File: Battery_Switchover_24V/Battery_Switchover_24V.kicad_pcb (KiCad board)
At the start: 2 copper layers, 260.5 x 131 mm, 105 parts, among them J1 USB_C_Receptacle_USB2.0_14P, M1 Fan, Q1 PZT2222AT1G, SW1 SW_Push, U10 ACS37002LMABTR-066B5, U11 LM60CIM3, U12 L5973D, U13 AMS1117-3.3, U14 OPA2197xD, U15 FDBL86066-F085, U2 FDBL86066-F085, U3 LPC11U14FBD48-201, U4 LM74610QDGKRQ1, U5 FDBL86066-F085, U6 LM74610QDGKRQ1, U7 FDBL86066-F085, U8 ACS37002LMABTR-066B5, U9 ACS37002LMABTR-066B5, Y1 12.000MHz

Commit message: Added 6 Pin ATX Connector
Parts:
- removed BT2, BT4, BT5, BT6: Battery_Cell, TerminalBlock_RND:TerminalBlock_RND_205-00023_1x02_P10.00mm_Horizontal
- added J10: 10845060, footprints:CONN_SDA_42002-xxxxx_06_MOL, F.Cu at (31.1, 127.3)
- added J11: 10845060, footprints:CONN_SDA_42002-xxxxx_06_MOL, F.Cu at (31.1, 149.4)
- added J3: 10845060, footprints:CONN_SDA_42002-xxxxx_06_MOL, F.Cu at (34.1, 35.5)
- added J4: 10845060, footprints:CONN_SDA_42002-xxxxx_06_MOL, F.Cu at (34.1, 57.6)
- added J5: 10845060, footprints:CONN_SDA_42002-xxxxx_06_MOL, F.Cu at (34.1, 79.7)
- added J6: 10845060, footprints:CONN_SDA_42002-xxxxx_06_MOL, F.Cu at (265.5, 95.6)
- added J7: 10845060, footprints:CONN_SDA_42002-xxxxx_06_MOL, F.Cu at (265.5, 121.3)
- added J8: 10845060, footprints:CONN_SDA_42002-xxxxx_06_MOL, F.Cu at (265.5, 147.1)
- added J9: 10845060, footprints:CONN_SDA_42002-xxxxx_06_MOL, F.Cu at (31.1, 105.3)
- J1: footprint Connector_USB:USB_C_Receptacle_G-Switch_GT-USB-7010ASV -> Connector_USB:USB_C_Receptacle_G-Switch_GT-USB-7051x
- moved C27 125.1 mm to (84.8, 72.2), turned to 0 degrees
- moved C28 121.5 mm to (88.1, 72.2), turned to 180 degrees
- moved C22 117.3 mm to (89.1, 75.7), turned to 0 degrees
- moved U8 113.0 mm to (86.3, 85.2), turned to 90 degrees
- moved R14 111.2 mm to (93.1, 77.7), turned to -90 degrees
- moved C26 103.9 mm to (104.3, 72.8), turned to 0 degrees
- moved C29 100.8 mm to (107.6, 72.8), turned to 180 degrees
- moved C24 96.7 mm to (108.3, 76.1), turned to 0 degrees
- moved R15 92.1 mm to (112.1, 77.0), turned to -90 degrees
- moved U9 89.2 mm to (105.8, 86.6), turned to 90 degrees
- moved C25 86.5 mm to (123.3, 73.7), turned to 0 degrees
- moved C30 84.2 mm to (126.5, 73.7), turned to 180 degrees
- moved C2 83.5 mm to (152.0, 96.3)
- moved C3 83.5 mm to (152.0, 98.5)
- moved C4 83.5 mm to (162.7, 87.8)
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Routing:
- net Net-(D6-A2): track 107.0 -> 0.00 mm
- net Vbatt: track 106.1 -> 0.00 mm
- net Net-(U3-USB_DM): track 42.2 -> 0.00 mm, vias 2 -> 0
- net Net-(U3-USB_DP): track 42.2 -> 0.00 mm
- net Net-(U15-G): track 33.0 -> 0.00 mm, vias 2 -> 0
- net +5V: track 20.0 -> 0.00 mm
- net Vin: track 15.3 -> 0.00 mm
- net Net-(U3-XTALIN): track 13.3 -> 0.00 mm
- net Net-(U3-XTALOUT): track 13.1 -> 0.00 mm
- net +3.3V: track 12.0 -> 0.00 mm
- net Net-(J1-D--PadA7): track 10.6 -> 0.00 mm
- net Net-(J1-CC1): track 10.2 -> 0.00 mm
- net VREF3: track 9.66 -> 0.00 mm
- net Net-(U6-VCAPH): track 9.19 -> 0.00 mm
- net Net-(U4-VCAPH): track 8.22 -> 0.00 mm
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- removed copper zone on F.Cu, net Load1
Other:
- board size 260.5 x 131 mm -> 260.5 x 89 mm

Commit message: Changed PCB size Changed output connector
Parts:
- removed BT3: Battery_Cell, TerminalBlock_RND:TerminalBlock_RND_205-00023_1x02_P10.00mm_Horizontal
- removed J10, J11, J3, J6, J7, J8, J9: 10845060, footprints:CONN_SDA_42002-xxxxx_06_MOL
- added J2: 430450612, footprints:CONN_SD-43045-005_06_MOL, F.Cu at (83.0, 110.0)
- added R20: 4K7, Resistor_SMD:R_0603_1608Metric, F.Cu at (124.7, 98.8)
- J4, J5: value 10845060 -> 430450612; footprint footprints:CONN_SDA_42002-xxxxx_06_MOL -> footprints:CONN_SD-43045-005_06_MOL
- moved C22 151.6 mm to (228.2, 136.0)
- moved C24 151.6 mm to (247.5, 136.4)
- moved C26 151.6 mm to (243.5, 133.2)
- moved C27 151.6 mm to (224.0, 132.5)
- moved C28 151.6 mm to (227.2, 132.5)
- moved C29 151.6 mm to (246.7, 133.2)
- moved R14 151.6 mm to (232.2, 138.0)
- moved R15 151.6 mm to (251.2, 137.4)
- moved U8 151.6 mm to (225.5, 145.5)
- moved U9 151.6 mm to (245.0, 146.9)
- moved U10 123.7 mm to (243.6, 83.4)
- moved J4 79.6 mm to (83.0, 120.4)
- moved R17 72.4 mm to (149.4, 75.6)
- moved D8 71.1 mm to (168.6, 110.7)
- moved J5 70.8 mm to (83.0, 130.8)
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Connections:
- J4 pad 1: GNDPWR2 -> GND
- J4 pad 2: GNDPWR2 -> GND
- J4 pad 3: GNDPWR2 -> GND
- J4 pad 4: Load2 -> Vsupply
- J4 pad 5: Load2 -> Vsupply
- J4 pad 6: Load2 -> Vsupply
- J5 pad 1: GNDPWR1 -> GND
- J5 pad 2: GNDPWR1 -> GND
- J5 pad 3: GNDPWR1 -> GND
- J5 pad 4: Load1 -> Vsupply
- J5 pad 5: Load1 -> Vsupply
- J5 pad 6: Load1 -> Vsupply
- U3 pad 18: unconnected-(U3-PIO1_23-Pad18) -> Temp_data
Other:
- board size 260.5 x 89 mm -> 150.1 x 89 mm

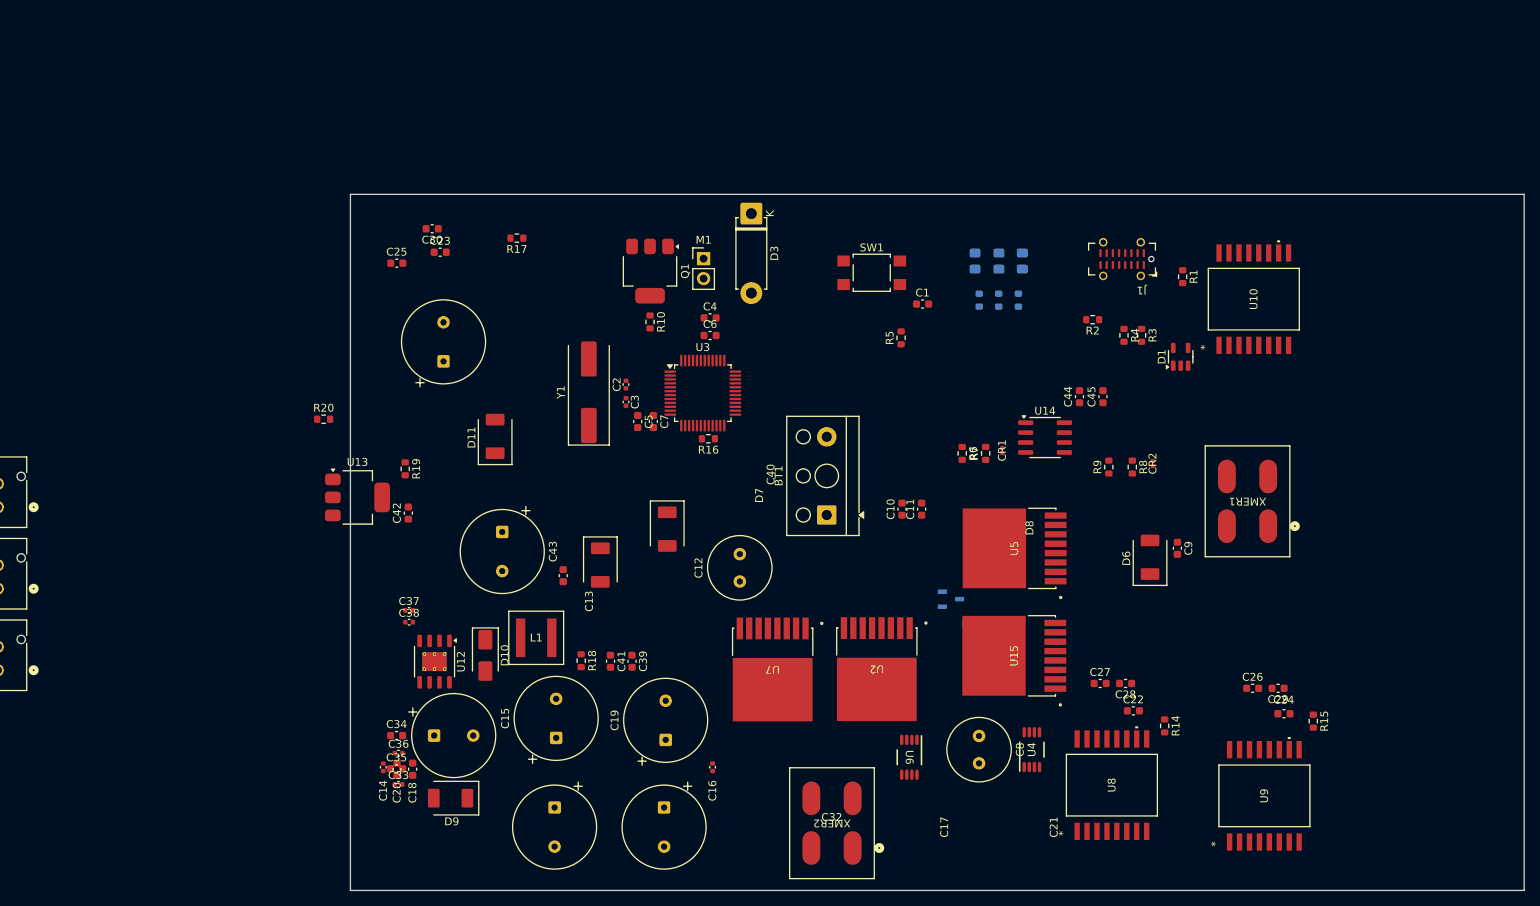
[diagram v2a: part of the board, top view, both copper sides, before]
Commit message: adding BMS and changed topology
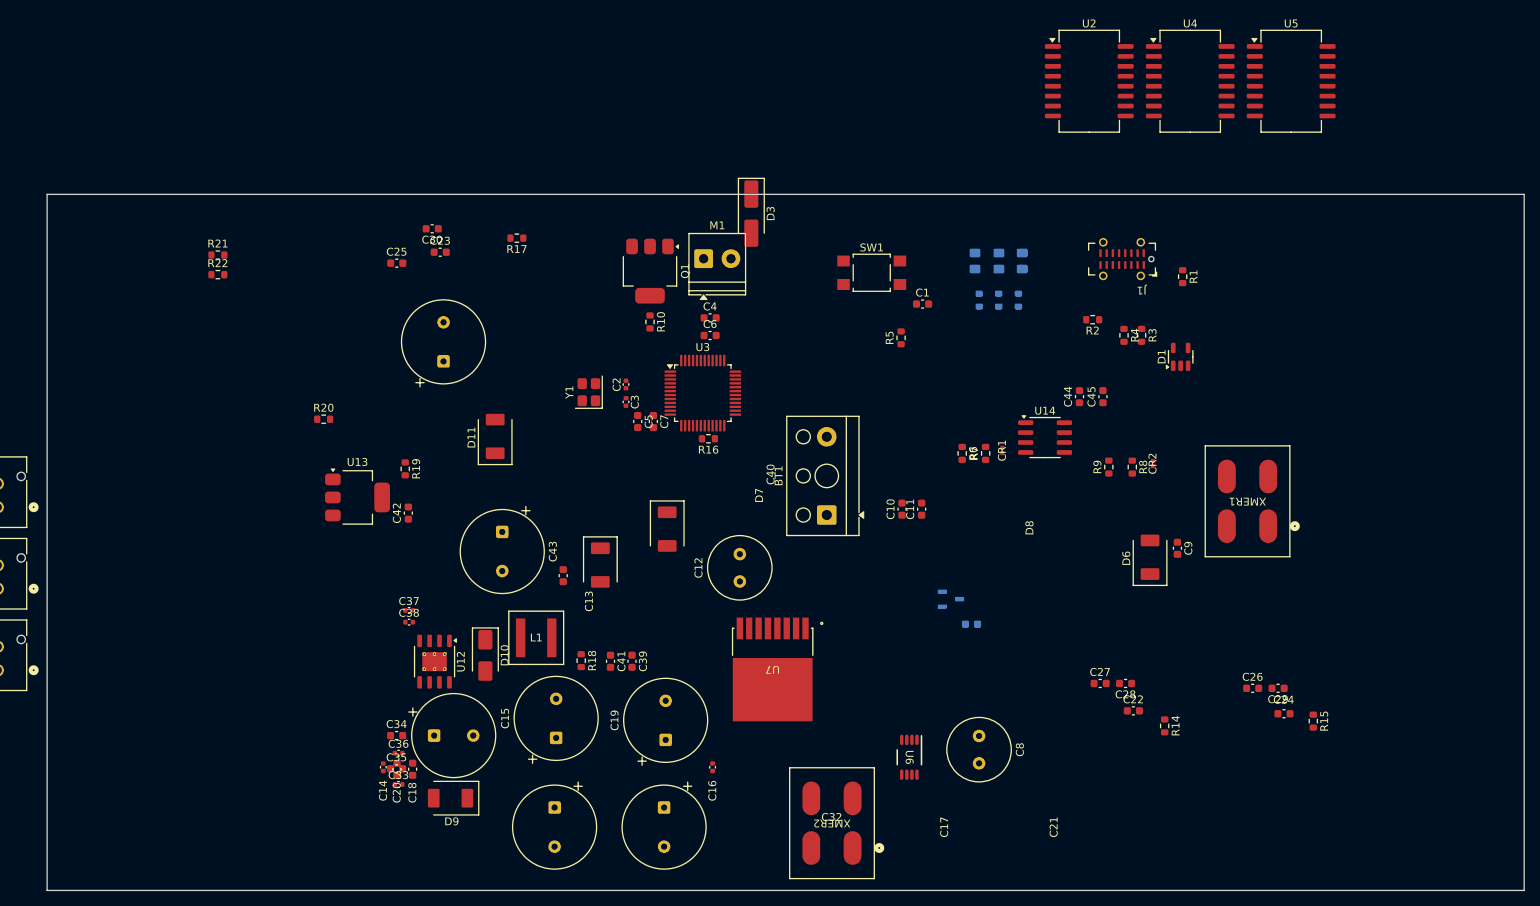
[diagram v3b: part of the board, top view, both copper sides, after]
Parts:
- removed U10, U8, U9: ACS37002LMABTR-066B5, footprints:SOICW16_MC_ALM
- removed U15: FDBL86066-F085, footprints:H-PSOF8L_ONS
- added R21: 4K7, Resistor_SMD:R_0603_1608Metric, F.Cu at (111.1, 77.8)
- added R22: 4K7, Resistor_SMD:R_0603_1608Metric, F.Cu at (111.1, 80.3)
- C1: value 1nF -> 10nF
- C6, C7: value 10uF -> 1uF
- D3: footprint Diode_THT:D_5W_P10.16mm_Horizontal -> Diode_SMD:D_SMA_Handsoldering
- M1: footprint Connector_PinHeader_2.54mm:PinHeader_1x02_P2.54mm_Vertical -> TerminalBlock_Phoenix:TerminalBlock_Phoenix_PT-1,5-2-3.5-H_1x02_P3.50mm_Horizontal
- R10: value 500 -> 10K
- R5: value 10K -> 1K
- U2, U5: value FDBL86066-F085 -> ACS37002; footprint footprints:H-PSOF8L_ONS -> Package_SO:SOIC-16W_7.5x12.8mm_P1.27mm
- U4: value LM74610QDGKRQ1 -> ACS37002; footprint footprints:DGK0008A_N -> Package_SO:SOIC-16W_7.5x12.8mm_P1.27mm
- Y1: footprint Crystal:Crystal_SMD_HC49-SD -> Crystal:Crystal_SMD_TXC_7M-4Pin_3.2x2.5mm
- moved U4 87.8 mm to (235.5, 55.5), turned to 0 degrees
- moved U2 79.9 mm to (222.6, 55.5), turned to 0 degrees
- moved U5 69.4 mm to (248.4, 55.5), turned to 0 degrees
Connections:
- C1 pad 1: Net-(C1-Pad1) -> RESET
- C8 pad 1: Net-(U4-VCAPH) -> unconnected-(C8-Pad1)
- C8 pad 2: Net-(U4-VCAPL) -> unconnected-(C8-Pad2)
- C9 pad 1: Net-(D6-A2) -> Net-(C9-Pad1)
- D1 pad 1: +5V -> Net-(D12-A)
- D6 pad 2: Net-(D6-A2) -> Vin
- J1 pad A4: +5V -> Net-(D12-A)
- J1 pad A9: +5V -> Net-(D12-A)
- J1 pad B4: +5V -> Net-(D12-A)
- J1 pad B9: +5V -> Net-(D12-A)
- R14 pad 2: Net-(U8-*OCF) -> Net-(U2-*OCF)
- R15 pad 2: Net-(U9-*OCF) -> Net-(U4-*OCF)
- R16 pad 2: Net-(U10-*OCF) -> Net-(U5-*OCF)
- R5 pad 1: RESET -> +3.3V
- R5 pad 2: Net-(C1-Pad1) -> RESET
- SW1 pad 1: 3.3V -> GND
- SW1 pad 2: Net-(C1-Pad1) -> RESET
- U2 pad 1: Net-(U2-G) -> Load1
- U2 pad 2: Vbatt -> Load1
- U2 pad 3: Vbatt -> Load1
- U2 pad 4: Vbatt -> Load1
- U2 pad 5: Vbatt -> GNDPWR1
- U2 pad 6: Vbatt -> GNDPWR1
- U2 pad 7: Vbatt -> GNDPWR1
- U2 pad 8: Vbatt -> GNDPWR1
- U2 pad 9: Net-(D6-A2) -> Net-(U2-*OCF)
- U4 pad 1: Net-(U4-VCAPL) -> Load2
- U4 pad 2: Net-(U15-G) -> Load2
- U4 pad 3: unconnected-(U4-NC-Pad3) -> Load2
- U4 pad 4: Net-(D6-A2) -> Load2
- U4 pad 5: unconnected-(U4-NC-Pad5) -> GNDPWR2
- U4 pad 6: Net-(U15-G) -> GNDPWR2
- U4 pad 7: Net-(U4-VCAPH) -> GNDPWR2
- U4 pad 8: Vbatt -> GNDPWR2
- U5 pad 1: Net-(U15-G) -> Load3
- U5 pad 2: Net-(D6-A2) -> Load3
- U5 pad 3: Net-(D6-A2) -> Load3
- U5 pad 4: Net-(D6-A2) -> Load3
- U5 pad 5: Net-(D6-A2) -> GNDPWR3
- U5 pad 6: Net-(D6-A2) -> GNDPWR3
- U5 pad 7: Net-(D6-A2) -> GNDPWR3
- U5 pad 8: Net-(D6-A2) -> GNDPWR3
- U5 pad 9: Vbatt -> Net-(U5-*OCF)
- U6 pad 2: Net-(U2-G) -> Net-(U6-GATE_DRIVE)
- U6 pad 6: Net-(U2-G) -> Net-(U6-GATE_DRIVE)
- U6 pad 8: Net-(D6-A2) -> Net-(U6-CATHODE)
- U7 pad 1: Net-(U2-G) -> Net-(U6-GATE_DRIVE)
- U7 pad 9: Net-(D6-A2) -> Net-(U6-CATHODE)
- XMER1 pad 4: Net-(D6-A2) -> Net-(C9-Pad1)
- XMER2 pad 1: Net-(D6-A2) -> Net-(U6-CATHODE)
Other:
- board size 150.1 x 89 mm -> 188.9 x 89 mm

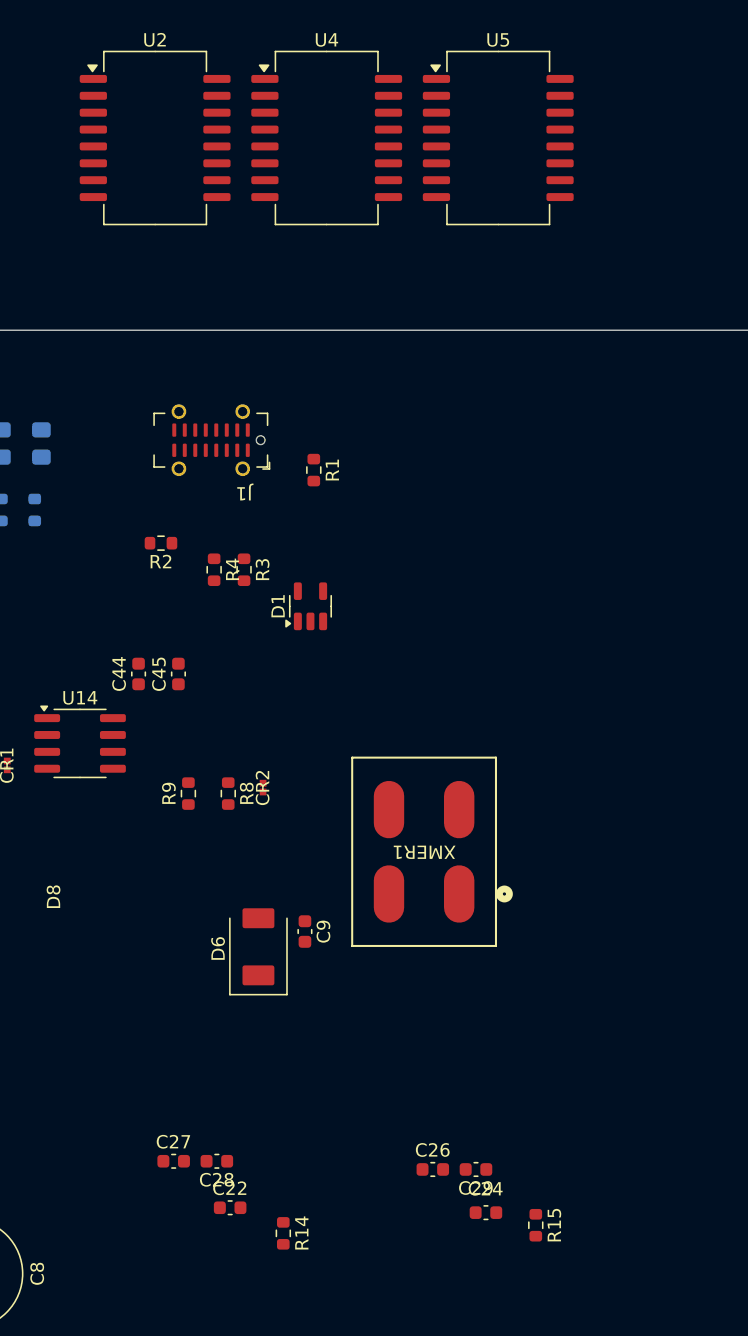
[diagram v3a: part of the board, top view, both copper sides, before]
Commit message: Changed current sensor (fewer analog pins), added extra adc
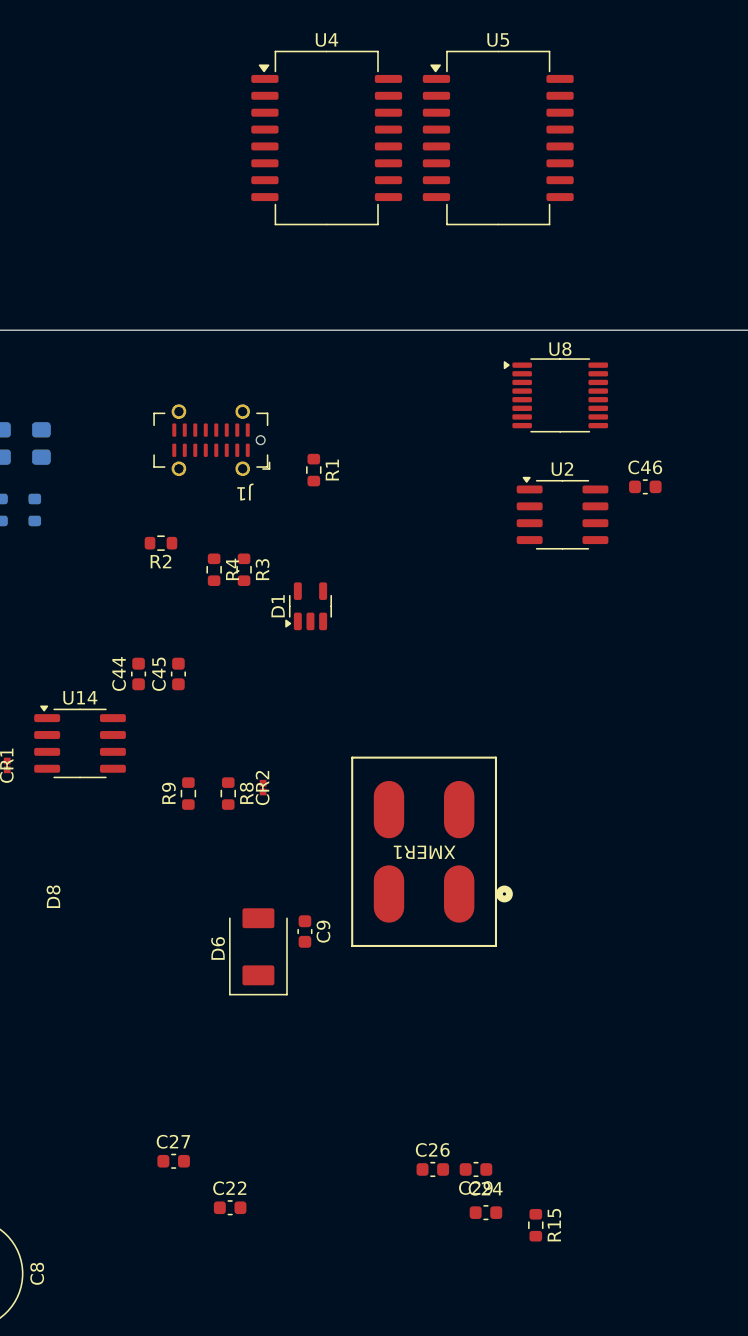
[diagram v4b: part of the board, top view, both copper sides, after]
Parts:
- removed C28: 6nF, Capacitor_SMD:C_0603_1608Metric
- removed R14: 100K, Resistor_SMD:R_0603_1608Metric
- added C46: 100nF, Capacitor_SMD:C_0603_1608Metric, F.Cu at (259.4, 81.8)
- added U8: ADS7830IPWR, Package_SO:TSSOP-16_4.4x5mm_P0.65mm, F.Cu at (253.0, 74.9)
- D3: value 1N4007 -> 1N4148
- U2: value ACS37002 -> ACS71240LLCBTR-010B3; footprint Package_SO:SOIC-16W_7.5x12.8mm_P1.27mm -> Package_SO:SOIC-8_3.9x4.9mm_P1.27mm
- moved U2 41.8 mm to (253.2, 83.9)
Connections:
- net Battery_Status renamed Battery_Status_LED
- net Fan_Status renamed Fan_Status_LED
- net Main_Voltage renamed Main_Voltage_LED
- C22 pad 2: +5V -> +3.3V
- C27 pad 2: VREF1 -> Net-(U2-ERR/FILTER)
- U2 pad 1: Load1 -> Load2
- U2 pad 2: Load1 -> Load2
- U2 pad 3: Load1 -> GNDPWR1
- U2 pad 4: Load1 -> GNDPWR1
- U2 pad 5: GNDPWR1 -> GND
- U2 pad 6: GNDPWR1 -> Net-(U2-ERR/FILTER)
- U2 pad 7: GNDPWR1 -> VIOUT1
- U2 pad 8: GNDPWR1 -> +3.3V
